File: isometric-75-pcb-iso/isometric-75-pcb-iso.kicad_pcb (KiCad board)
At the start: 2 copper layers, 263 parts, among them J1 Conn_01x05, SW1 SW_Push, SW2 Rotary_Encoder_Switch, U1 STM32F072CBTx

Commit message: wired switches and leds
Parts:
- moved R82 320.3 mm to (285.0, 86.8)
- moved R81 316.4 mm to (285.0, 67.8)
- moved R80 313.3 mm to (285.0, 48.8)
- moved R79 312.0 mm to (285.0, 29.8)
- moved R78 308.0 mm to (261.2, 110.5)
- moved R77 302.5 mm to (261.2, 91.5)
- moved R60 228.0 mm to (204.2, 29.8)
- moved R57 226.7 mm to (190.0, 86.8)
- moved R61 220.9 mm to (194.8, 48.8)
- moved C9 212.5 mm to (155.0, 119.2)
- moved SW1 208.4 mm to (165.1, 125.6)
- moved R56 204.0 mm to (180.5, 67.8)
- moved C4 201.0 mm to (160.9, 105.3)
- moved R85 199.5 mm to (151.6, 119.0)
- moved J1 199.2 mm to (145.3, 97.9), turned to 90 degrees
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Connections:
- C6 pad 1: +3V3 -> Net-(C6-Pad1)
- R1 pad 2: Net-(R1-Pad2) -> Net-(C6-Pad1)
- U1 pad 9: Net-(R1-Pad2) -> Net-(C6-Pad1)
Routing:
- net LED+: track 0.00 -> 1848.2 mm
- net LED-: track 0.00 -> 1736.1 mm
- net ROW0: track 0.00 -> 302.9 mm
- net ROW5: track 0.00 -> 302.4 mm
- net ROW1: track 0.00 -> 301.9 mm
- net ROW4: track 0.00 -> 300.0 mm
- net ROW3: track 0.00 -> 298.6 mm
- net ROW2: track 0.00 -> 293.3 mm
- net COL13: track 0.00 -> 118.4 mm
- net COL6: track 0.00 -> 117.7 mm
- net COL11: track 0.00 -> 117.2 mm
- net COL2: track 0.00 -> 115.9 mm
- net COL14: track 0.00 -> 112.4 mm
- net COL10: track 0.00 -> 111.6 mm
- net COL15: track 0.00 -> 111.5 mm
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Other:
- board outline added: 308.8 x 123.5 mm
- net class Default: clearance 0.2 -> 0.1905; trace_width 0.25 -> 0.254
- net class Power added: clearance 0.1905, trace_width 0.381, via_dia 0.8, via_drill 0.4
- rule trace_clearance: 0.2 -> 0.1905
- rule trace_min: 0.2 -> 0.2032
- rule via_min_size: 0.4 -> 0.6

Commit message: continued the pcb
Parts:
- removed C1, C2, C3, C4, C5, C6: 100n, Capacitor_SMD:C_0402_1005Metric
- removed C7: 1u, Capacitor_SMD:C_0402_1005Metric
- removed J1: Conn_01x05, Connector_JST:JST_SH_SM05B-SRSS-TB_1x05-1MP_P1.00mm_Horizontal
- removed MX36: MX-LED, MX_Only:MXOnly-6.25U
- removed R1: 100, Resistor_SMD:R_0402_1005Metric
- removed R84, R85: 10k, Resistor_SMD:R_0402_1005Metric
- removed U1: STM32F072CBTx, Package_QFP:LQFP-48_7x7mm_P0.5mm
- added C101: 1u, Capacitor_SMD:C_0402_1005Metric, B.Cu at (138.9, 95.9)
- added C102: 100n, Capacitor_SMD:C_0402_1005Metric, B.Cu at (163.8, 99.9)
- added C103: 1u, Capacitor_SMD:C_0402_1005Metric, B.Cu at (142.0, 92.5)
- added C104: 100n, Capacitor_SMD:C_0402_1005Metric, B.Cu at (160.6, 93.6)
- added C105: 100n, Capacitor_SMD:C_0402_1005Metric, B.Cu at (163.7, 96.1)
- added C106: 100n, Capacitor_SMD:C_0402_1005Metric, B.Cu at (165.0, 100.9)
- added C107: 100n, Capacitor_SMD:C_0402_1005Metric, B.Cu at (154.8, 105.3)
- added C108: 100n, Capacitor_SMD:C_0402_1005Metric, B.Cu at (151.9, 96.6)
- added C109: 1u, Capacitor_SMD:C_0402_1005Metric, B.Cu at (150.6, 96.6)
- added C110: 100n, Capacitor_SMD:C_0402_1005Metric, B.Cu at (154.1, 110.6)
- added J101: Conn_01x05, Connector_JST:JST_SH_SM05B-SRSS-TB_1x05-1MP_P1.00mm_Horizontal, B.Cu at (140.7, 107.8)
- added J102: Conn_01x06, Connector_JST:JST_SH_SM06B-SRSS-TB_1x06-1MP_P1.00mm_Horizontal, B.Cu at (181.2, 107.8)
- added MX236: MX-LED, MX_Only:MXOnly-6.25U, F.Cu at (121.1, 99.8)
- added Q101: AO3400A, Package_TO_SOT_SMD:SOT-23, B.Cu at (132.7, 106.3)
- added R101: 100, Resistor_SMD:R_0402_1005Metric, B.Cu at (165.0, 103.0)
- added R102: 10k, Resistor_SMD:R_0402_1005Metric, B.Cu at (155.3, 110.6)
- added R103: 10k, Resistor_SMD:R_0402_1005Metric, B.Cu at (154.8, 108.5)
- added R104: 100, Resistor_SMD:R_0402_1005Metric, B.Cu at (146.2, 98.2)
- added R283: 10k, Resistor_SMD:R_0402_1005Metric, B.Cu at (171.2, 102.6)
- added R284: 10k, Resistor_SMD:R_0402_1005Metric, B.Cu at (173.1, 102.6)
- added U101: XC6206P332MR, Package_TO_SOT_SMD:SOT-23, B.Cu at (139.4, 93.3)
- added U102: STM32F072CBTx, Package_QFP:LQFP-48_7x7mm_P0.5mm, B.Cu at (157.7, 99.4)
- moved SW101 44.1 mm to (133.2, 95.1), turned to 270 degrees
- moved C202 26.1 mm to (173.1, 100.4), turned to 90 degrees
- moved C201 21.3 mm to (171.2, 100.4), turned to 270 degrees
- renumbered C8 to C201, C9 to C202, D1 to D201, D2 to D202, D3 to D203, D4 to D204, D5 to D205, D6 to D206, D7 to D207, D8 to D208, D9 to D209, D10 to D210, D11 to D211, D12 to D212, D13 to D213, D14 to D214, D15 to D215, D16 to D216, D17 to D217, D18 to D218, D19 to D219, D20 to D220, D21 to D221, D22 to D222, D23 to D223, D24 to D224, D25 to D225, D26 to D226, D27 to D227, D28 to D228, D29 to D229, D30 to D230, D31 to D231, D32 to D232, D33 to D233, D34 to D234, D35 to D235, D36 to D236, D37 to D237, D38 to D238, D39 to D239, D40 to D240, D41 to D241, D42 to D242, D43 to D243, D44 to D244, D45 to D245, D46 to D246, D47 to D247, D48 to D248, D49 to D249, D50 to D250, D51 to D251, D52 to D252, D53 to D253, D54 to D254, D55 to D255, D56 to D256, D57 to D257, D58 to D258, D59 to D259, D60 to D260, D61 to D261, D62 to D262, D63 to D263, D64 to D264, D65 to D265, D66 to D266, D67 to D267, D68 to D268, D69 to D269, D70 to D270, D71 to D271, D72 to D272, D73 to D273, D74 to D274, D75 to D275, D76 to D276, D77 to D277, D78 to D278, D79 to D279, D80 to D280, D81 to D281, D82 to D282, D83 to D283, MX1 to MX201, MX2 to MX202, MX3 to MX203, MX4 to MX204, MX5 to MX205, MX6 to MX206, MX7 to MX207, MX8 to MX208, MX9 to MX209, MX10 to MX210, MX11 to MX211, MX12 to MX212, MX13 to MX213, MX14 to MX214, MX15 to MX215, MX16 to MX216, MX17 to MX217, MX18 to MX218, MX19 to MX219, MX20 to MX220, MX21 to MX221, MX22 to MX222, MX23 to MX223, MX24 to MX224, MX25 to MX225, MX26 to MX226, MX27 to MX227, MX28 to MX228, MX29 to MX229, MX30 to MX230, MX31 to MX231, MX32 to MX232, MX33 to MX233, MX34 to MX234, MX35 to MX235, MX37 to MX237, MX38 to MX238, MX39 to MX239, MX40 to MX240, MX41 to MX241, MX42 to MX242, MX43 to MX243, MX44 to MX244, MX45 to MX245, MX46 to MX246, MX47 to MX247, MX48 to MX248, MX49 to MX249, MX50 to MX250, MX51 to MX251, MX52 to MX252, MX53 to MX253, MX54 to MX254, MX55 to MX255, MX56 to MX256, MX57 to MX257, MX58 to MX258, MX59 to MX259, MX60 to MX260, MX61 to MX261, MX62 to MX262, MX63 to MX263, MX64 to MX264, MX65 to MX265, MX66 to MX266, MX67 to MX267, MX68 to MX268, MX69 to MX269, MX70 to MX270, MX71 to MX271, MX72 to MX272, MX73 to MX273, MX74 to MX274, MX75 to MX275, MX76 to MX276, MX77 to MX277, MX78 to MX278, MX79 to MX279, MX80 to MX280, MX81 to MX281, MX82 to MX282, R2 to R201, R3 to R202, R4 to R203, R5 to R204, R6 to R205, R7 to R206, R8 to R207, R9 to R208, R10 to R209, R11 to R210, R12 to R211, R13 to R212, R14 to R213, R15 to R214, R16 to R215, R17 to R216, R18 to R217, R19 to R218, R20 to R219, R21 to R220, R22 to R221, R23 to R222, R24 to R223, R25 to R224, R26 to R225, R27 to R226, R28 to R227, R29 to R228, R30 to R229, R31 to R230, R32 to R231, R33 to R232, R34 to R233, R35 to R234, R36 to R235, R37 to R236, R38 to R237, R39 to R238, R40 to R239, R41 to R240, R42 to R241, R43 to R242, R44 to R243, R45 to R244, R46 to R245, R47 to R246, R48 to R247, R49 to R248, R50 to R249, R51 to R250, R52 to R251, R53 to R252, R54 to R253, R55 to R254, R56 to R255, R57 to R256, R58 to R257, R59 to R258, R60 to R259, R61 to R260, R62 to R261, R63 to R262, R64 to R263, R65 to R264, R66 to R265, R67 to R266, R68 to R267, R69 to R268, R70 to R269, R71 to R270, R72 to R271, R73 to R272, R74 to R273, R75 to R274, R76 to R275, R77 to R276, R78 to R277, R79 to R278, R80 to R279, R81 to R280, R82 to R281, R83 to R282, SW1 to SW101, SW2 to SW201
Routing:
- net LED+: track 1848.2 -> 1986.0 mm, vias 0 -> 2
- net LED-: track 1736.1 -> 1822.0 mm
- net GND: track 34.4 -> 81.0 mm
- net Net-(C102-Pad1): track 1.79 -> 47.7 mm
- net SPI_MOSI: track 0.00 -> 29.8 mm
- net SPI_MISO: track 0.00 -> 27.8 mm
- net SPI_SCK: track 0.00 -> 25.9 mm
- net USB-D-: track 0.00 -> 25.0 mm
- net USB-D+: track 0.00 -> 24.0 mm
- net SPI_NSS: track 0.00 -> 23.9 mm
- net Net-(Q101-Pad1): track 0.00 -> 16.2 mm, vias 0 -> 2
- net Vsense: track 0.00 -> 15.5 mm, vias 0 -> 2
- net +3V3: track 52.6 -> 66.7 mm
- net Net-(C110-Pad1): track 0.00 -> 9.09 mm
- net LED_PWM: track 0.00 -> 7.11 mm
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
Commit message: more pcb wiring
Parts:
- added C111: 1u, Capacitor_SMD:C_0603_1608Metric, B.Cu at (129.3, 105.5)
- added C112: 1u, Capacitor_SMD:C_0603_1608Metric, B.Cu at (135.6, 93.4)
- added C113: 100n, Capacitor_SMD:C_0402_1005Metric, B.Cu at (158.6, 93.2)
- added R106: 10k, Resistor_SMD:R_0402_1005Metric, B.Cu at (158.6, 91.9)
- added SW102: BOOT, random-keyboard-parts:SKQG-1155865, B.Cu at (91.4, 96.9)
- C101, C103: footprint Capacitor_SMD:C_0402_1005Metric -> Capacitor_SMD:C_0603_1608Metric
- R201, R202, R203, R204, R205, R206, R207, R208, R209, R210, R211, R212, R213, R214, R215, R216, R217, R218, R219, R220, R221, R222, R223, R224, R225, R226, R227, R228, R229, R230, R231, R232, R233, R234, R235, R236, R237, R238, R239, R240, R241, R242, R243, R244, R245, R246, R247, R248, R249, R250, R251, R252, R253, R254, R255, R256, R257, R258, R259, R260, R261, R262, R263, R264, R265, R266, R267, R268, R269, R270, R271, R272, R273, R274, R275, R276, R277, R278, R279, R280, R281, R282, R283, R284: footprint Resistor_SMD:R_0402_1005Metric -> Resistor_SMD:R_0603_1608Metric
- SW101: value SW_Push -> RST
- moved SW101 53.4 mm to (79.9, 96.9)
- moved R104 14.0 mm to (133.5, 104.0)
- moved C101 8.67 mm to (130.3, 96.6)
- moved U101 8.67 mm to (130.8, 94.1)
- moved C103 8.31 mm to (133.7, 93.4)
- moved R102 5.44 mm to (150.3, 108.6), turned to 0 degrees
- moved C110 5.01 mm to (150.3, 107.3), turned to 0 degrees
- moved R284 4.94 mm to (169.9, 98.8), turned to 180 degrees
- moved R103 2.44 mm to (152.4, 108.1), turned to 90 degrees
- moved C201 1.79 mm to (172.7, 101.4)
- moved R283 1.59 mm to (170.0, 101.6), turned to 0 degrees
- moved C202 1.45 mm to (172.7, 99.0), turned to 270 degrees
- moved Q101 0.25 mm to (132.7, 106.6)
- moved R245 0.13 mm to (142.5, 67.8)
- moved R225 0.11 mm to (66.5, 67.8)
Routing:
- net GND: track 81.0 -> 411.7 mm
- net ROTB: track 1.19 -> 241.6 mm
- net ROTA: track 1.19 -> 240.5 mm
- net Net-(C113-Pad1): track 0.00 -> 75.7 mm
- net +3V3: track 66.7 -> 128.1 mm
- net Net-(C102-Pad1): track 47.7 -> 98.3 mm
- net LED_PWM: track 7.11 -> 22.2 mm, vias 0 -> 2
- net Net-(Q101-Pad1): track 16.2 -> 1.88 mm, vias 2 -> 0
- net LED-: track 1822.0 -> 1809.9 mm
- net LED+: track 1986.0 -> 1997.2 mm
- net Vsense: track 15.5 -> 7.57 mm
- net ROW5: track 302.4 -> 298.6 mm
- net Net-(C110-Pad1): track 9.09 -> 12.9 mm
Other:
- net class Power: trace_width 0.381 -> 0.254

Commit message: connecting rows
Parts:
- moved R101 2.80 mm to (167.6, 102.1)
- moved C102 1.27 mm to (165.1, 99.9)
- moved C106 1.27 mm to (166.2, 100.9)
- moved C107 0.13 mm to (154.7, 105.3)
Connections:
- U102 pad 10: Net-(U102-Pad10) -> ROTB
- U102 pad 11: Net-(U102-Pad11) -> ROTA
- U102 pad 13: Net-(U102-Pad13) -> COL11
- U102 pad 18: Net-(U102-Pad18) -> COL12
- U102 pad 20: Net-(U102-Pad20) -> COL13
- U102 pad 21: Net-(U102-Pad21) -> COL14
- U102 pad 22: Net-(U102-Pad22) -> COL15
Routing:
- net COL15: track 113.0 -> 251.7 mm, vias 0 -> 1
- net COL12: track 70.1 -> 201.2 mm, vias 0 -> 1
- net COL14: track 113.2 -> 230.7 mm, vias 0 -> 1
- net COL13: track 119.8 -> 216.5 mm, vias 0 -> 1
- net COL11: track 118.2 -> 189.1 mm, vias 0 -> 1
- net ROTB: track 241.6 -> 254.5 mm, vias 0 -> 2
- net ROTA: track 240.5 -> 253.1 mm, vias 0 -> 2
- net Net-(C102-Pad1): track 98.3 -> 107.2 mm
- net Net-(C106-Pad1): track 4.47 -> 6.14 mm
- net Net-(C113-Pad1): track 75.7 -> 77.1 mm
- net +3V3: track 128.1 -> 126.8 mm

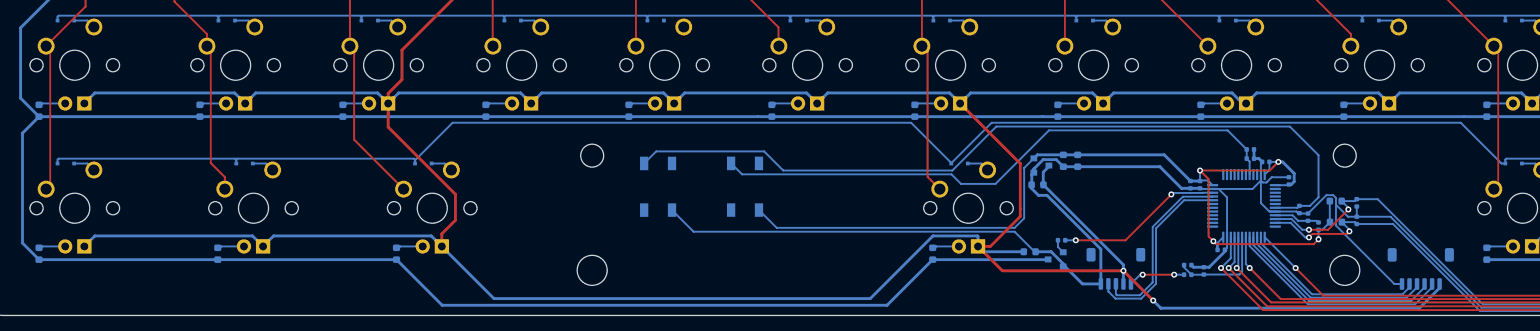
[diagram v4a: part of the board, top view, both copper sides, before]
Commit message: finished wiring cols, changed jlc connector color
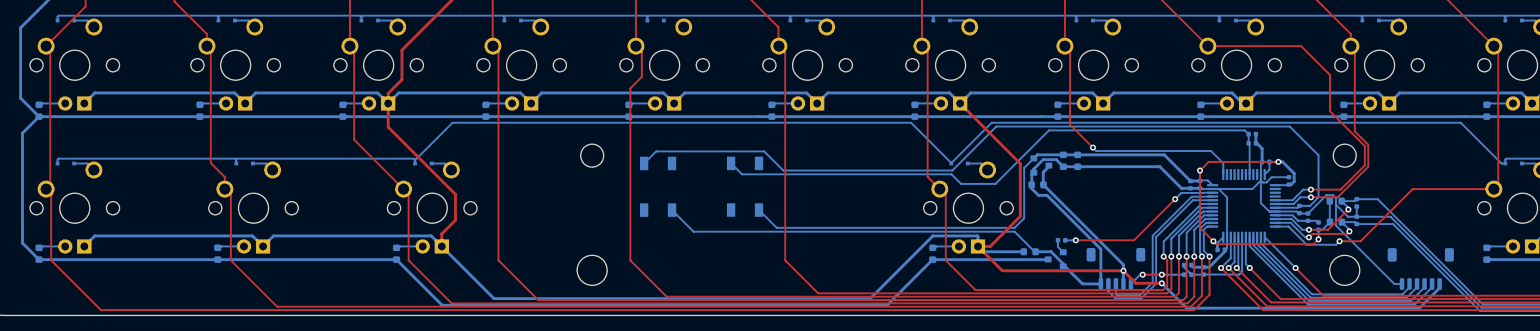
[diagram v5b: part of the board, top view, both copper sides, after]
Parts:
- J_101: renamed from J101; value Conn_01x05 -> USB
- J_102: renamed from J102; value Conn_01x06 -> SPI
- moved C113 2.05 mm to (158.8, 91.1)
- moved R106 2.05 mm to (158.8, 89.9)
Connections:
- U102 pad 12: Net-(U102-Pad12) -> COL10
- U102 pad 25: Net-(U102-Pad25) -> COL0
- U102 pad 26: Net-(U102-Pad26) -> COL1
- U102 pad 27: Net-(U102-Pad27) -> COL2
- U102 pad 28: Net-(U102-Pad28) -> COL3
- U102 pad 29: Net-(U102-Pad29) -> COL4
- U102 pad 30: Net-(U102-Pad30) -> COL5
- U102 pad 31: Net-(U102-Pad31) -> COL6
- U102 pad 37: Net-(U102-Pad37) -> COL7
- U102 pad 5: Net-(U102-Pad5) -> COL8
- U102 pad 6: Net-(U102-Pad6) -> COL9
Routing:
- net COL0: track 106.0 -> 283.5 mm, vias 0 -> 1
- net COL1: track 105.1 -> 258.1 mm, vias 0 -> 1
- net COL3: track 99.0 -> 234.5 mm, vias 0 -> 1
- net COL2: track 117.4 -> 246.5 mm, vias 0 -> 1
- net COL4: track 95.2 -> 213.1 mm, vias 0 -> 1
- net COL5: track 67.3 -> 163.3 mm, vias 0 -> 1
- net COL6: track 118.7 -> 174.4 mm, vias 0 -> 1
- net COL8: track 95.0 -> 140.5 mm, vias 0 -> 1
- net COL7: track 96.6 -> 131.3 mm, vias 0 -> 1
- net COL10: track 112.4 -> 145.6 mm, vias 0 -> 1
- net COL9: track 95.0 -> 126.4 mm, vias 0 -> 1
- net GND: track 411.9 -> 413.5 mm
- net Net-(C113-Pad1): track 77.1 -> 78.5 mm
- net USB-D+: track 24.0 -> 23.4 mm
- net USB-D-: track 25.0 -> 24.3 mm
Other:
- net class Power: trace_width 0.254 -> 0.381

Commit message: added underglow
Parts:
- added C301: 100n, Capacitor_SMD:C_0402_1005Metric, B.Cu at (129.8, 110.5)
- added C302: 100n, Capacitor_SMD:C_0402_1005Metric, B.Cu at (86.5, 106.7)
- added C303: 100n, Capacitor_SMD:C_0402_1005Metric, B.Cu at (54.1, 110.3)
- added C304: 100n, Capacitor_SMD:C_0402_1005Metric, B.Cu at (11.1, 106.8)
- added C305: 100n, Capacitor_SMD:C_0402_1005Metric, B.Cu at (10.1, 8.89)
- added C306: 100n, Capacitor_SMD:C_0402_1005Metric, B.Cu at (47.9, 8.89)
- added C307: 100n, Capacitor_SMD:C_0402_1005Metric, B.Cu at (85.9, 8.89)
- added C308: 100n, Capacitor_SMD:C_0402_1005Metric, B.Cu at (123.7, 8.89)
- added C309: 100n, Capacitor_SMD:C_0402_1005Metric, B.Cu at (161.7, 8.89)
- added C310: 100n, Capacitor_SMD:C_0402_1005Metric, B.Cu at (199.6, 8.89)
- added C311: 100n, Capacitor_SMD:C_0402_1005Metric, B.Cu at (137.4, 95.5)
- added C312: 100n, Capacitor_SMD:C_0402_1005Metric, B.Cu at (237.5, 8.89)
- added C313: 100n, Capacitor_SMD:C_0402_1005Metric, B.Cu at (275.5, 8.89)
- added C314: 100n, Capacitor_SMD:C_0402_1005Metric, B.Cu at (275.5, 49.4)
- added C315: 100n, Capacitor_SMD:C_0402_1005Metric, B.Cu at (275.5, 92.6)
- added C316: 100n, Capacitor_SMD:C_0402_1005Metric, B.Cu at (237.2, 93.0)
- added C317: 100n, Capacitor_SMD:C_0402_1005Metric, B.Cu at (199.7, 106.3)
- added C318: 100n, Capacitor_SMD:C_0402_1005Metric, B.Cu at (19.6, 51.6)
- added D301: SK6812MINI, LED_SMD:LED_SK6812MINI_PLCC4_3.5x3.5mm_P1.75mm, B.Cu at (125.6, 110.0)
- added D302: SK6812MINI, LED_SMD:LED_SK6812MINI_PLCC4_3.5x3.5mm_P1.75mm, B.Cu at (87.7, 109.8)
- added D303: SK6812MINI, LED_SMD:LED_SK6812MINI_PLCC4_3.5x3.5mm_P1.75mm, B.Cu at (49.8, 109.8)
- added D304: SK6812MINI, LED_SMD:LED_SK6812MINI_PLCC4_3.5x3.5mm_P1.75mm, B.Cu at (11.9, 109.8)
- added D305: SK6812MINI, LED_SMD:LED_SK6812MINI_PLCC4_3.5x3.5mm_P1.75mm, B.Cu at (11.9, 11.9)
- added D306: SK6812MINI, LED_SMD:LED_SK6812MINI_PLCC4_3.5x3.5mm_P1.75mm, B.Cu at (49.8, 11.9)
- added D307: SK6812MINI, LED_SMD:LED_SK6812MINI_PLCC4_3.5x3.5mm_P1.75mm, B.Cu at (87.7, 11.9)
- added D308: SK6812MINI, LED_SMD:LED_SK6812MINI_PLCC4_3.5x3.5mm_P1.75mm, B.Cu at (125.6, 11.9)
- added D309: SK6812MINI, LED_SMD:LED_SK6812MINI_PLCC4_3.5x3.5mm_P1.75mm, B.Cu at (163.5, 11.9)
- added D310: SK6812MINI, LED_SMD:LED_SK6812MINI_PLCC4_3.5x3.5mm_P1.75mm, B.Cu at (201.5, 11.9)
- added D311: SK6812MINI, LED_SMD:LED_SK6812MINI_PLCC4_3.5x3.5mm_P1.75mm, B.Cu at (239.4, 11.9)
- added D312: SK6812MINI, LED_SMD:LED_SK6812MINI_PLCC4_3.5x3.5mm_P1.75mm, B.Cu at (277.3, 11.9)
- added D313: SK6812MINI, LED_SMD:LED_SK6812MINI_PLCC4_3.5x3.5mm_P1.75mm, B.Cu at (277.3, 52.6)
- added D314: SK6812MINI, LED_SMD:LED_SK6812MINI_PLCC4_3.5x3.5mm_P1.75mm, B.Cu at (277.3, 95.6)
- added D315: SK6812MINI, LED_SMD:LED_SK6812MINI_PLCC4_3.5x3.5mm_P1.75mm, B.Cu at (238.1, 96.2)
- added D316: SK6812MINI, LED_SMD:LED_SK6812MINI_PLCC4_3.5x3.5mm_P1.75mm, B.Cu at (201.5, 109.2)
- added D317: SK6812MINI, LED_SMD:LED_SK6812MINI_PLCC4_3.5x3.5mm_P1.75mm, B.Cu at (16.4, 52.4)
- added U301: 74LVC1G125, Package_TO_SOT_SMD:SOT-23-5, B.Cu at (138.4, 98.1)
- moved C105 1.62 mm to (162.8, 94.7), turned to 180 degrees
- moved C113 0.25 mm to (158.8, 90.9)
- moved MX246 0.25 mm to (156.8, 80.5)
- moved R106 0.25 mm to (158.8, 89.7)
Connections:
- U102 pad 2: Net-(U102-Pad2) -> ROW3
- U102 pad 3: Net-(U102-Pad3) -> ROW4
- U102 pad 38: Net-(U102-Pad38) -> UGLED
- U102 pad 4: Net-(U102-Pad4) -> ROW5
- U102 pad 43: Net-(U102-Pad43) -> ROW0
- U102 pad 45: Net-(U102-Pad45) -> ROW1
- U102 pad 46: Net-(U102-Pad46) -> ROW2
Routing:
- net GND: track 413.5 -> 1193.1 mm, vias 0 -> 9
- net LED+: track 1997.2 -> 2747.6 mm, vias 2 -> 13
- net ROW0: track 302.9 -> 420.1 mm, vias 0 -> 2
- net ROW1: track 301.9 -> 393.6 mm, vias 0 -> 2
- net ROW2: track 293.3 -> 363.2 mm, vias 0 -> 2
- net Net-(D304-Pad1): track 0.00 -> 63.2 mm, vias 0 -> 2
- net ROW3: track 298.6 -> 361.7 mm, vias 0 -> 2
- net Net-(D313-Pad1): track 0.00 -> 50.6 mm, vias 0 -> 2
- net Net-(D312-Pad1): track 0.00 -> 48.4 mm, vias 0 -> 2
- net Net-(D315-Pad1): track 0.00 -> 43.8 mm, vias 0 -> 2
- net Net-(D314-Pad1): track 0.00 -> 42.2 mm, vias 0 -> 2
- net Net-(D305-Pad3): track 0.00 -> 40.2 mm, vias 0 -> 2
- net ROW4: track 300.0 -> 339.7 mm, vias 0 -> 2
- net Net-(D302-Pad1): track 0.00 -> 35.3 mm
- net Net-(D301-Pad1): track 0.00 -> 35.2 mm
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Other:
- net class Power: trace_width 0.381 -> 0.508

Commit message: added ground planes, various minor fixes
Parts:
- added J101: Conn_01x06_Male, Connector_PinHeader_2.54mm:PinHeader_1x06_P2.54mm_Vertical, F.Cu at (147.5, 96.5)
- R201, R202, R203, R204, R205, R206, R207, R208, R209, R210, R211, R212, R213, R214, R215, R216, R217, R218, R219, R220, R221, R222, R223, R224, R225, R226, R227, R228, R229, R230, R231, R232, R233, R234, R235, R236, R237, R238, R239, R240, R241, R242, R243, R244, R245, R246, R247, R248, R249, R250, R251, R252, R253, R254, R255, R256, R257, R258, R259, R260, R261, R262, R263, R264, R265, R266, R267, R268, R269, R270, R271, R272, R273, R274, R275, R276, R277, R278, R279, R280, R281, R282: value 330 -> 680
- moved C311 8.07 mm to (130.3, 99.3)
- moved U301 8.07 mm to (131.3, 101.9)
- moved R104 1.33 mm to (134.5, 103.1)
- moved C303 0.68 mm to (54.1, 111.0)
- moved MX246 0.25 mm to (156.8, 80.8)
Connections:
- J_101 pad 2: USB-D- -> USB-D+
- J_101 pad 3: USB-D+ -> USB-D-
- U102 pad 39: Net-(U102-Pad39) -> ROW0
- U102 pad 43: ROW0 -> Net-(J101-Pad6)
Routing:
- net GND: track 1193.1 -> 915.9 mm, vias 9 -> 11
- net Net-(J101-Pad6): track 0.00 -> 30.7 mm, vias 0 -> 1
- net Net-(J101-Pad5): track 0.00 -> 28.1 mm, vias 0 -> 1
- net Net-(J101-Pad4): track 0.00 -> 21.9 mm, vias 0 -> 1
- net Net-(J101-Pad3): track 0.00 -> 18.2 mm, vias 0 -> 1
- net UGLED: track 21.3 -> 32.5 mm
- net +3V3: track 124.2 -> 132.7 mm
- net Net-(D301-Pad3): track 16.9 -> 9.49 mm
- net LED+: track 2747.6 -> 2754.3 mm, vias 13 -> 14
- net USB-D-: track 24.3 -> 22.3 mm
- net COL0: track 283.5 -> 281.6 mm
- net COL1: track 258.1 -> 256.3 mm
- net ROW3: track 361.7 -> 363.4 mm
- net COL2: track 246.5 -> 244.9 mm
- net COL3: track 234.5 -> 233.1 mm
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- added copper zone on B.Cu, net GND
- added copper zone on F.Cu, net GND
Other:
- rule trace_min: 0.2032 -> 0.254

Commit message: cosmethical changes, fixed a footprint collision
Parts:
- removed J_101: USB, Connector_JST:JST_SH_SM05B-SRSS-TB_1x05-1MP_P1.00mm_Horizontal
- added J101: USB, Connector_JST:JST_SH_SM05B-SRSS-TB_1x05-1MP_P1.00mm_Horizontal, B.Cu at (140.7, 107.8)
- J103: renamed from J101; moved to B.Cu
- moved R284 0.51 mm to (169.4, 98.8)
- moved C103 0.44 mm to (133.7, 93.0)
- moved C109 0.44 mm to (135.6, 93.0)
- turned J103 to 90 degrees
- renumbered C111 to C102, C107 to C106, C108 to C107, C109 to C108, C112 to C109, C102 to C110, C106 to C111, C113 to C112, C110 to C113, C311 to C301, C301 to C302, C302 to C303, C303 to C304, C304 to C305, C318 to C306, C305 to C307, C306 to C308, C307 to C309, C308 to C310, C309 to C311, C310 to C312, C312 to C313, C313 to C314, C314 to C315, C315 to C316, C316 to C317, C317 to C318, D317 to D305, D305 to D306, D306 to D307, D307 to D308, D308 to D309, D309 to D310, D310 to D311, D311 to D312, D312 to D313, D313 to D314, D314 to D315, D315 to D316, D316 to D317, J_102 to J102, R104 to R101, R101 to R102, R106 to R103, R102 to R104, R103 to R105
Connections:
- net Net-(J101-Pad3) renamed PB4
- net Net-(J101-Pad4) renamed PB5
- net Net-(J101-Pad5) renamed PB6_TX1
- net Net-(J101-Pad6) renamed PB7_RX1
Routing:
- net GND: track 915.9 -> 874.4 mm, vias 11 -> 12
- net +3V3: track 132.7 -> 138.4 mm, vias 4 -> 5
- net LED+: track 2754.3 -> 2749.4 mm
- net LED-: track 1813.4 -> 1815.8 mm
- net ROTA: track 252.1 -> 250.0 mm
- net COL6: track 174.3 -> 172.5 mm
- net USB-D-: track 22.3 -> 21.7 mm
- net ROTB: track 253.6 -> 253.1 mm
- net Vsense: vias 2 -> 0
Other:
- net class USB added: clearance 0.1905, trace_width 0.254, via_dia 0.8, via_drill 0.4
- board text added: "BOOT"
- board text added: "RST"
- board text added: "SPI"
- board text added: "USB"
- board text added: "isometric75 rev 1.0 github.com/ebastler/isometric-75 mpwr.xyz"
